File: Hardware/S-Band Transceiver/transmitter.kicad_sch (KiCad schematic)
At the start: 41 parts, among them J5 SMA, U10 TSS-53LNB3+, U11 DCW-22-332+, U12 ADL5906, U7 DAT-31A+, U8 PE44820, U9 SN74LVC1G125DCK

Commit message: Updates to schematic
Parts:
- C57, C60, C63, C64, C70: value 10nF -> 10000pF
- J5: value SMA -> SMA-J-P-H-ST-EM1; Digikey (none) -> SAM8857-ND
- U10: Digikey (none) -> 3157-TSS-53LNB3+CT-ND
- U11: Digikey (none) -> 3157-DCW-22-332+CT-ND
- U12: Digikey (none) -> 505-ADL5906ACPZN-R7CT-ND
- U7: Digikey (none) -> 3157-DAT-31A-PP+CT-ND
- U8: Digikey (none) -> 1046-1144-1-ND
- U9: Digikey (none) -> 296-11604-1-ND
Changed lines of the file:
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@@
 			)
 		)
+		(property "Digikey" "1046-1144-1-ND"
+			(at 118.11 55.88 0)
+			(effects
+				(font
+					(size 1.27 1.27)
+				)
+				(hide yes)
+			)
+		)
 		(pin "17"
 		)
@@
 			)
 		)
+		(property "Digikey" "505-ADL5906ACPZN-R7CT-ND"
+			(at 227.33 121.92 0)
+			(effects
+				(font
+					(size 1.27 1.27)
+				)
+				(hide yes)
+			)
+		)
 		(pin "13"
 		)
@@
 			)
 		)
-		(property "Value" "10nF"
+		(property "Value" "10000pF"
 			(at 210.8263 115.57 90)
 			(effects
@@
 			)
 		)
-		(property "Value" "10nF"
+		(property "Value" "10000pF"
 			(at 147.3263 52.07 90)
 			(effects
@@
 			)
 		)
+		(property "Digikey" "3157-DCW-22-332+CT-ND"
+			(at 212.09 55.88 0)
+			(effects
+				(font
+					(size 1.27 1.27)
+				)
+				(hide yes)
+			)
+		)
 		(pin "3"
 		)
@@
 			)
 		)
+		(property "Digikey" "296-11604-1-ND"
+			(at 161.29 31.75 0)
+			(effects
+				(font
+					(size 1.27 1.27)
+				)
+				(hide yes)
+			)
+		)
 		(pin "1"
 		)
@@
 			)
 		)
-		(property "Value" "SMA"
+		(property "Value" "SMA-J-P-H-ST-EM1"
 			(at 249.936 57.404 0)
 			(effects
@@
 			)
 		)
-		(property "Datasheet" " ~"
+		(property "Datasheet" "https://mm.digikey.com/Volume0/opasdata/d220001/medias/docus/6129/sma-j-p-x-st-em1-mkt.pdf"
 			(at 247.65 55.88 0)
 			(effects
@@
 			)
 		)
+		(property "Digikey" "SAM8857-ND"
+			(at 247.65 55.88 0)
+			(effects
+				(font
+					(size 1.27 1.27)
+				)
+				(hide yes)
+			)
+		)
 		(pin "1"
 		)
@@
 			)
 		)
+		(property "Digikey" "3157-TSS-53LNB3+CT-ND"
+			(at 176.53 55.88 0)
+			(effects
+				(font
+					(size 1.27 1.27)
+				)
+				(hide yes)
+			)
+		)
 		(pin "8"
 		)
@@
 			)
 		)
-		(property "Value" "10nF"
+		(property "Value" "10000pF"
 			(at 208.28 130.8162 0)
 			(effects
@@
 			)
 		)
+		(property "Digikey" "3157-DAT-31A-PP+CT-ND"
+			(at 67.31 55.88 0)
+			(effects
+				(font
+					(size 1.27 1.27)
+				)
+				(hide yes)
+			)
+		)
 		(pin "12"
 		)
@@
 			)
 		)
-		(property "Value" "10nF"
+		(property "Value" "10000pF"
 			(at 233.6863 52.07 90)
 			(effects
@@
 			)
 		)
-		(property "Value" "10nF"
+		(property "Value" "10000pF"
 			(at 92.7163 52.07 90)
 			(effects

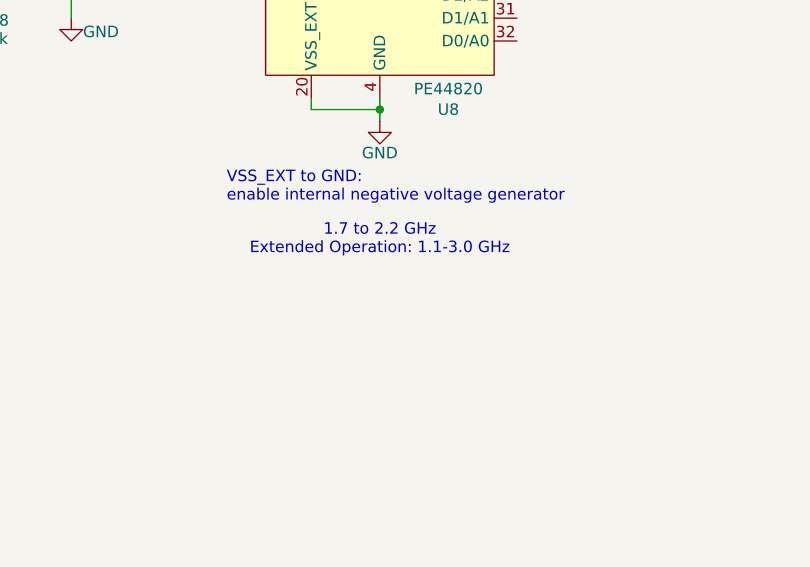
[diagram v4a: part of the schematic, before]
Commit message: Updating notes in schematic
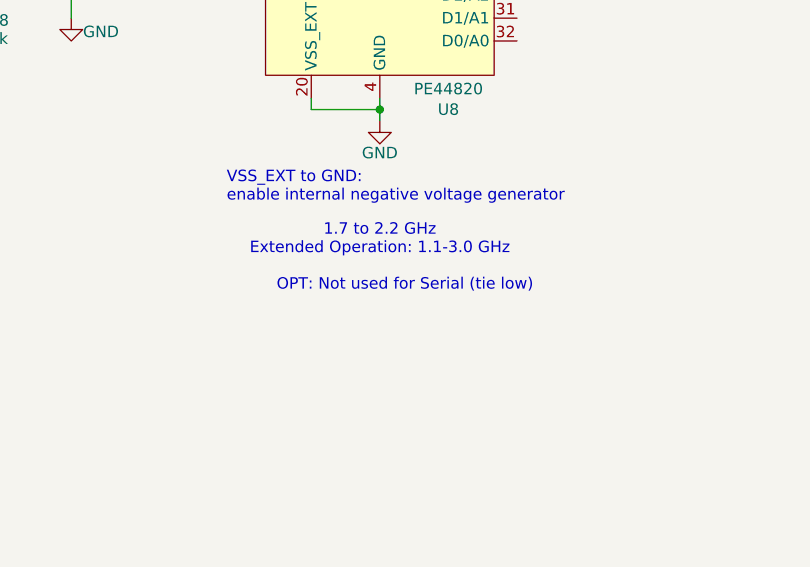
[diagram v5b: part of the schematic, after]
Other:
- note added: "OPT: Not used for Serial (tie low)"
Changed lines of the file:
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@@
+		)
+	)
+	(text "OPT: Not used for Serial (tie low)"
+		(exclude_from_sim no)
+		(at 120.904 113.538 0)
+		(effects
+			(font
+				(size 1.27 1.27)
+			)
 		)
 	)

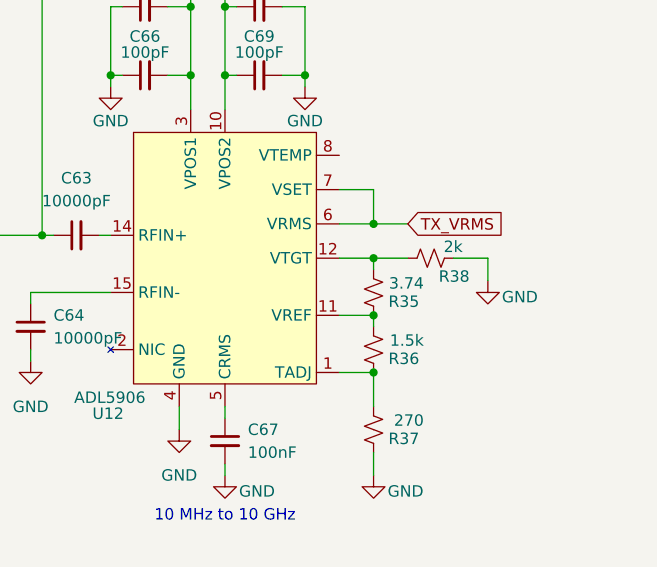
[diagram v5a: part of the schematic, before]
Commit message: Updates to BOM
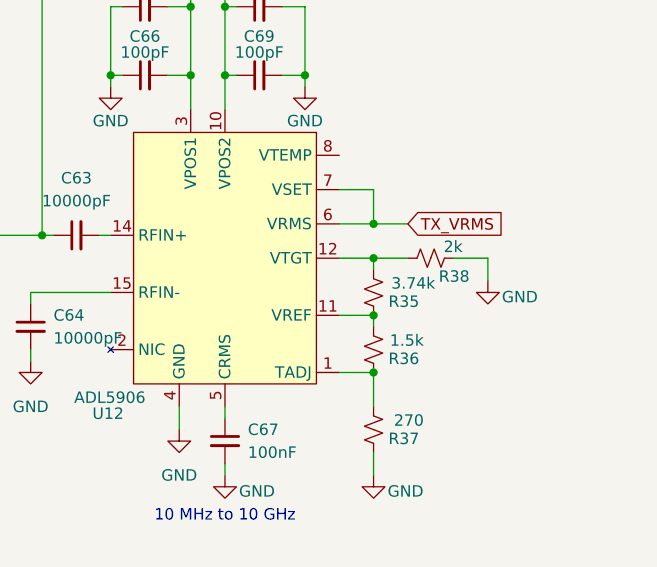
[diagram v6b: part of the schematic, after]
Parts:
- R35: value 3.74 -> 3.74k
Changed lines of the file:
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@@
 			)
 		)
-		(property "Value" "3.74"
-			(at 249.428 124.714 0)
+		(property "Value" "3.74k"
+			(at 250.698 124.714 0)
 			(effects
 				(font

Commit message: updating values
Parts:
- C62: value 10pF -> 100pF
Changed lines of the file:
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@@
 			)
 		)
-		(property "Value" "10pF"
+		(property "Value" "100pF"
 			(at 192.278 40.386 90)
 			(effects

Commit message: Fixing issues in schematic
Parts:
- added R67: 1k, Resistor_SMD:R_0603_1608Metric, symbol Device:R_Small_US
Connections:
- net GND: now also R67.1
- net at U9.1: now also R67.2
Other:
- note added: "NOTE: ~{OE} Pulled high to disable"
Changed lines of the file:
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@@
 	(wire
 		(pts
+			(xy 171.45 20.32) (xy 171.45 21.59)
+		)
+		(stroke
+			(width 0)
+			(type default)
+		)
+	)
+	(wire
+		(pts
 			(xy 125.73 43.18) (xy 125.73 44.45)
 		)
@@
 	(wire
 		(pts
+			(xy 161.29 20.32) (xy 165.1 20.32)
+		)
+		(stroke
+			(width 0)
+			(type default)
+		)
+	)
+	(wire
+		(pts
 			(xy 133.35 63.5) (xy 135.89 63.5)
 		)
@@
 	(wire
 		(pts
+			(xy 170.18 20.32) (xy 171.45 20.32)
+		)
+		(stroke
+			(width 0)
+			(type default)
+		)
+	)
+	(wire
+		(pts
 			(xy 133.35 66.04) (xy 135.89 66.04)
 		)
@@
 	(wire
 		(pts
+			(xy 161.29 21.59) (xy 161.29 20.32)
+		)
+		(stroke
+			(width 0)
+			(type default)
+		)
+	)
+	(wire
+		(pts
 			(xy 82.55 34.29) (xy 82.55 40.64)
 		)
@@
 		)
 	)
+	(text "NOTE: ~{OE} Pulled high to disable"
+		(exclude_from_sim no)
+		(at 177.8 13.97 0)
+		(effects
+			(font
+				(size 1.27 1.27)
+			)
+		)
+	)
 	(text "10 MHz to 10 GHz"
 		(exclude_from_sim no)
@@
 		)
 		(property "Value" "SN74LVC1G125DCK"
-			(at 145.034 25.908 0)
+			(at 142.24 27.686 0)
 			(effects
 				(font
@@
 	)
 	(symbol
+		(lib_id "power:GND")
+		(at 171.45 21.59 0)
+		(unit 1)
+		(exclude_from_sim no)
+		(in_bom yes)
+		(on_board yes)
+		(dnp no)
+		(property "Reference" "#PWR0144"
+			(at 171.45 27.94 0)
+			(effects
+				(font
+					(size 1.27 1.27)
+				)
+				(hide yes)
+			)
+		)
+		(property "Value" "GND"
+			(at 171.45 25.146 0)
+			(effects
+				(font
+					(size 1.27 1.27)
+				)
+			)
+		)
+		(property "Footprint" ""
+			(at 171.45 21.59 0)
+			(effects
+				(font
+					(size 1.27 1.27)
+				)
+				(hide yes)
+			)
+		)
+		(property "Datasheet" ""
+			(at 171.45 21.59 0)
+			(effects
+				(font
+					(size 1.27 1.27)
+				)
+				(hide yes)
+			)
+		)
+		(property "Description" "Power symbol creates a global label with name \"GND\" , ground"
+			(at 171.45 21.59 0)
+			(effects
+				(font
+					(size 1.27 1.27)
+				)
+				(hide yes)
+			)
+		)
+		(pin "1"
+		)
+		(instances
+			(project "S-Band Transceiver"
+				(path "/811f57cf-e3df-4fba-aff9-353adc85299e/bd41cfbd-cb46-4539-92e1-7ba2287bca8a"
+					(reference "#PWR0144")
+					(unit 1)
+				)
+			)
+		)
+	)
+	(symbol
 		(lib_id "Device:R_Small_US")
 		(at 172.72 44.45 90)
@@
 					(unit 1)
 				)
+			)
+		)
+	)
+	(symbol
+		(lib_id "Device:R_Small_US")
+		(at 167.64 20.32 270)
+		(unit 1)
+		(exclude_from_sim no)
+		(in_bom yes)
+		(on_board yes)
+		(dnp no)
+		(property "Reference" "R67"
+			(at 169.164 19.05 90)
+			(effects
+				(font
+					(size 1.27 1.27)
+				)
+				(justify left)
+			)
+		)
+		(property "Value" "1k"
+			(at 162.56 19.05 90)
+			(effects
+				(font
+					(size 1.27 1.27)
+				)
+				(justify left)
+			)
+		)
+		(property "Footprint" "Resistor_SMD:R_0603_1608Metric"
+			(at 167.64 20.32 0)
+			(effects
+				(font
+					(size 1.27 1.27)
+				)
+				(hide yes)
+			)
+		)
+		(property "Datasheet" "~"
+			(at 167.64 20.32 0)
+			(effects
+				(font
+					(size 1.27 1.27)
+				)
+				(hide yes)
+			)
+		)
+		(property "Description" "Resistor, small US symbol"
+			(at 167.64 20.32 0)
+			(effects
+				(font
+					(size 1.27 1.27)
+				)
+				(hide yes)
+			)
+		)
+		(pin "1"
+		)
+		(pin "2"
+		)
+		(instances
+			(project "S-Band Transceiver"
+				(path "/811f57cf-e3df-4fba-aff9-353adc85299e/bd41cfbd-cb46-4539-92e1-7ba2287bca8a"
+					(reference "R67")
+					(unit 1)
+				)
